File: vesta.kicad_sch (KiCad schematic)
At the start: 60 parts, among them J1 Solar Panel, J2 Solar Panel, J3 Conn_ARM_SWD_TagConnect_TC203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, U1 STM32WL55CCU6, U2 BQ24074RGTR, U3 TPS63900DSKR, U4 BME688_C3664478, U6 PE4259-63, X1 Q13FC1350000400, X2 X201632MMB4SI

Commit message: feat: updating the references and adding the logo
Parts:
- U2: footprint Package_DFN_QFN:MPS_QFN-16_3x3mm_P0.5mm -> JLCImport:BQ24074RGTR
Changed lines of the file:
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@@
 			)
 		)
-		(property "Footprint" "Package_DFN_QFN:MPS_QFN-16_3x3mm_P0.5mm"
+		(property "Footprint" "JLCImport:BQ24074RGTR"
 			(at 316.23 96.52 0)
 			(hide yes)

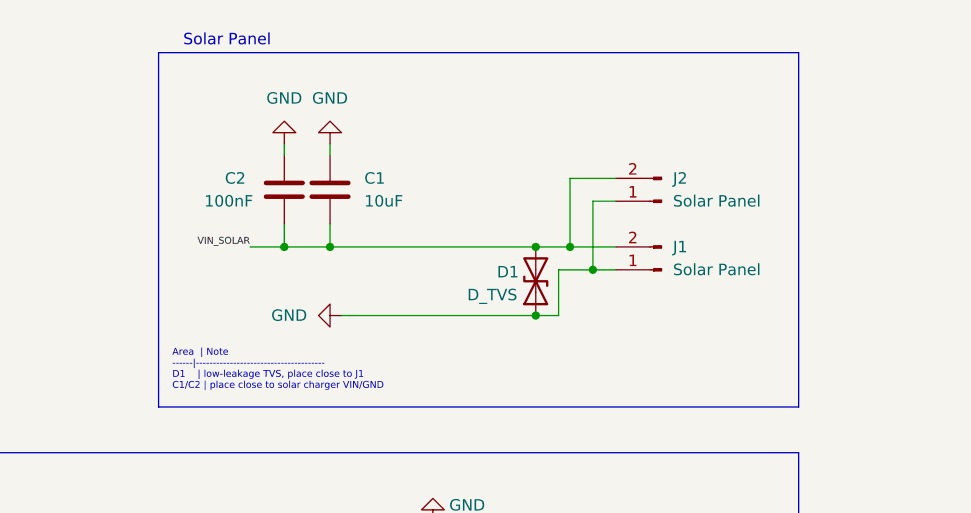
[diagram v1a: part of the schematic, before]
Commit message: feat: reverting the polarity on the batteries inputs
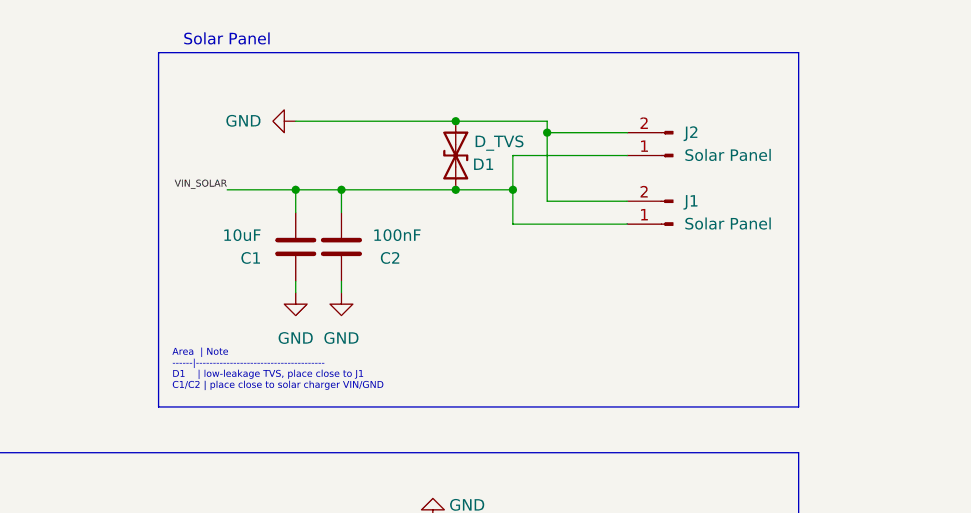
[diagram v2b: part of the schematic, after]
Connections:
- net GND: now also J1.2 (Pin_2), J2.2 (Pin_2); no longer J1.1 (Pin_1), J2.1 (Pin_1)
- net VIN_SOLAR: now also J1.1 (Pin_1), J2.1 (Pin_1); no longer J1.2 (Pin_2), J2.2 (Pin_2)
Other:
- moved on the sheet: C1, C2, D1, J1, J2

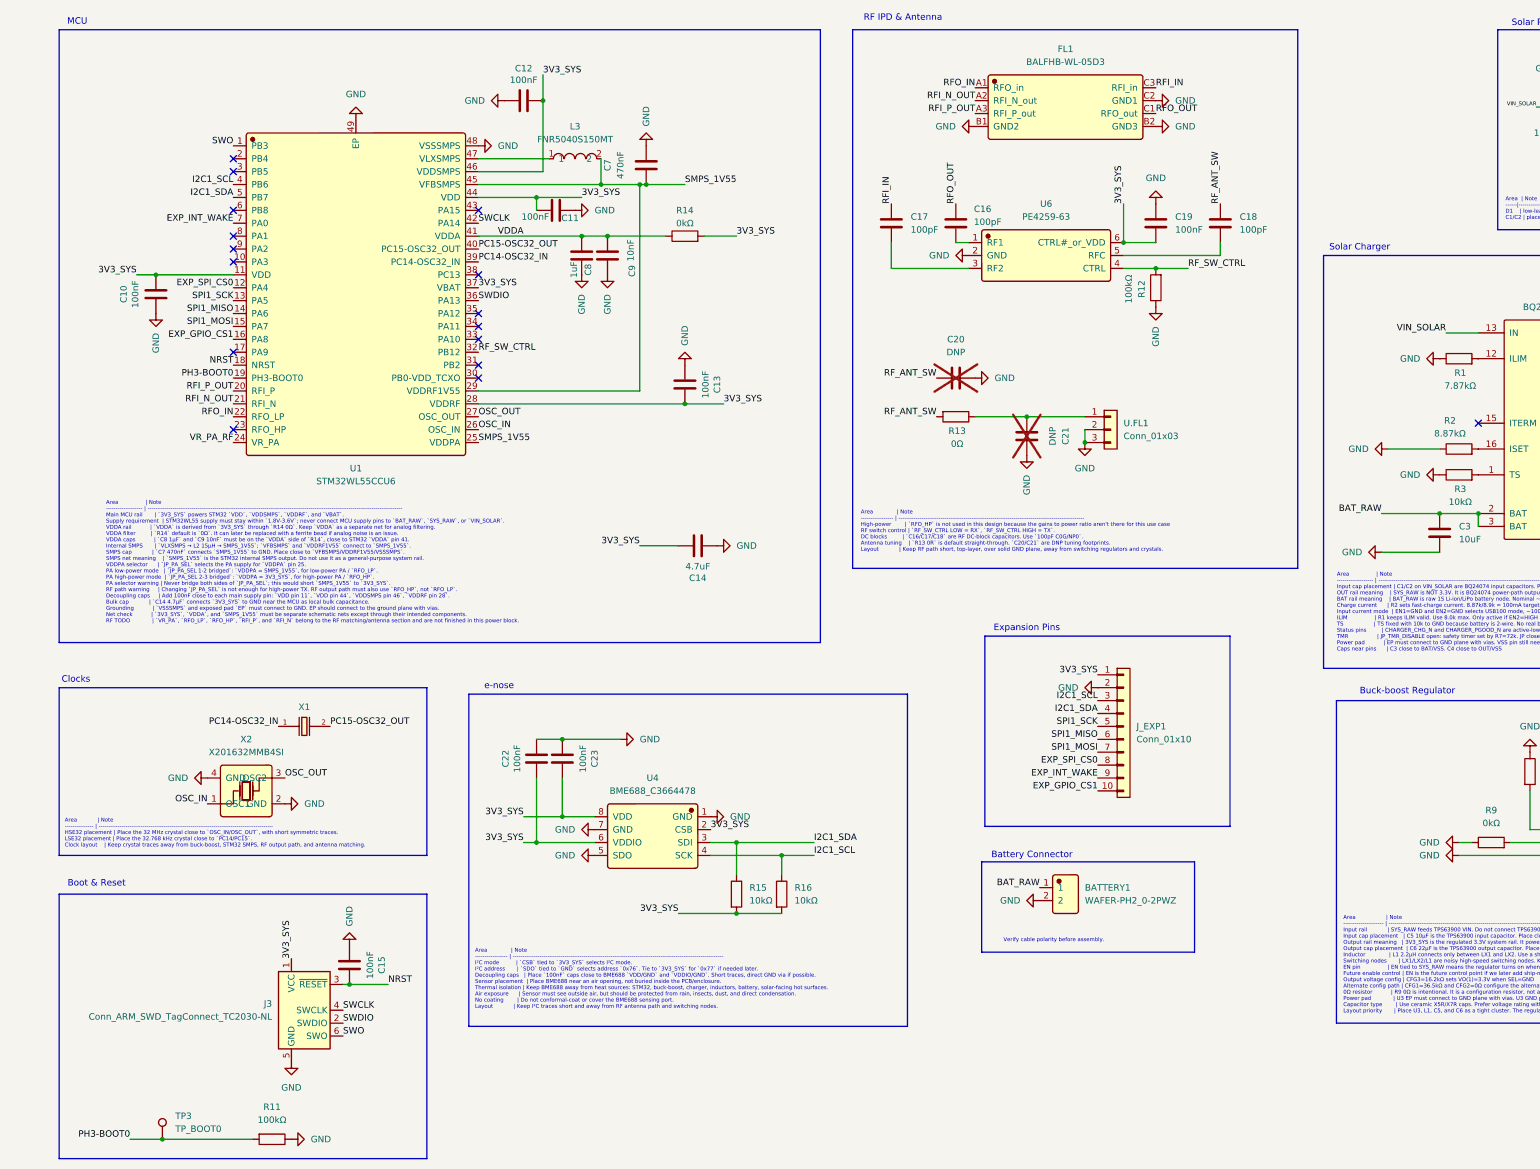
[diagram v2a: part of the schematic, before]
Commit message: feat: changing the MCU and antenna for a pre-certified module
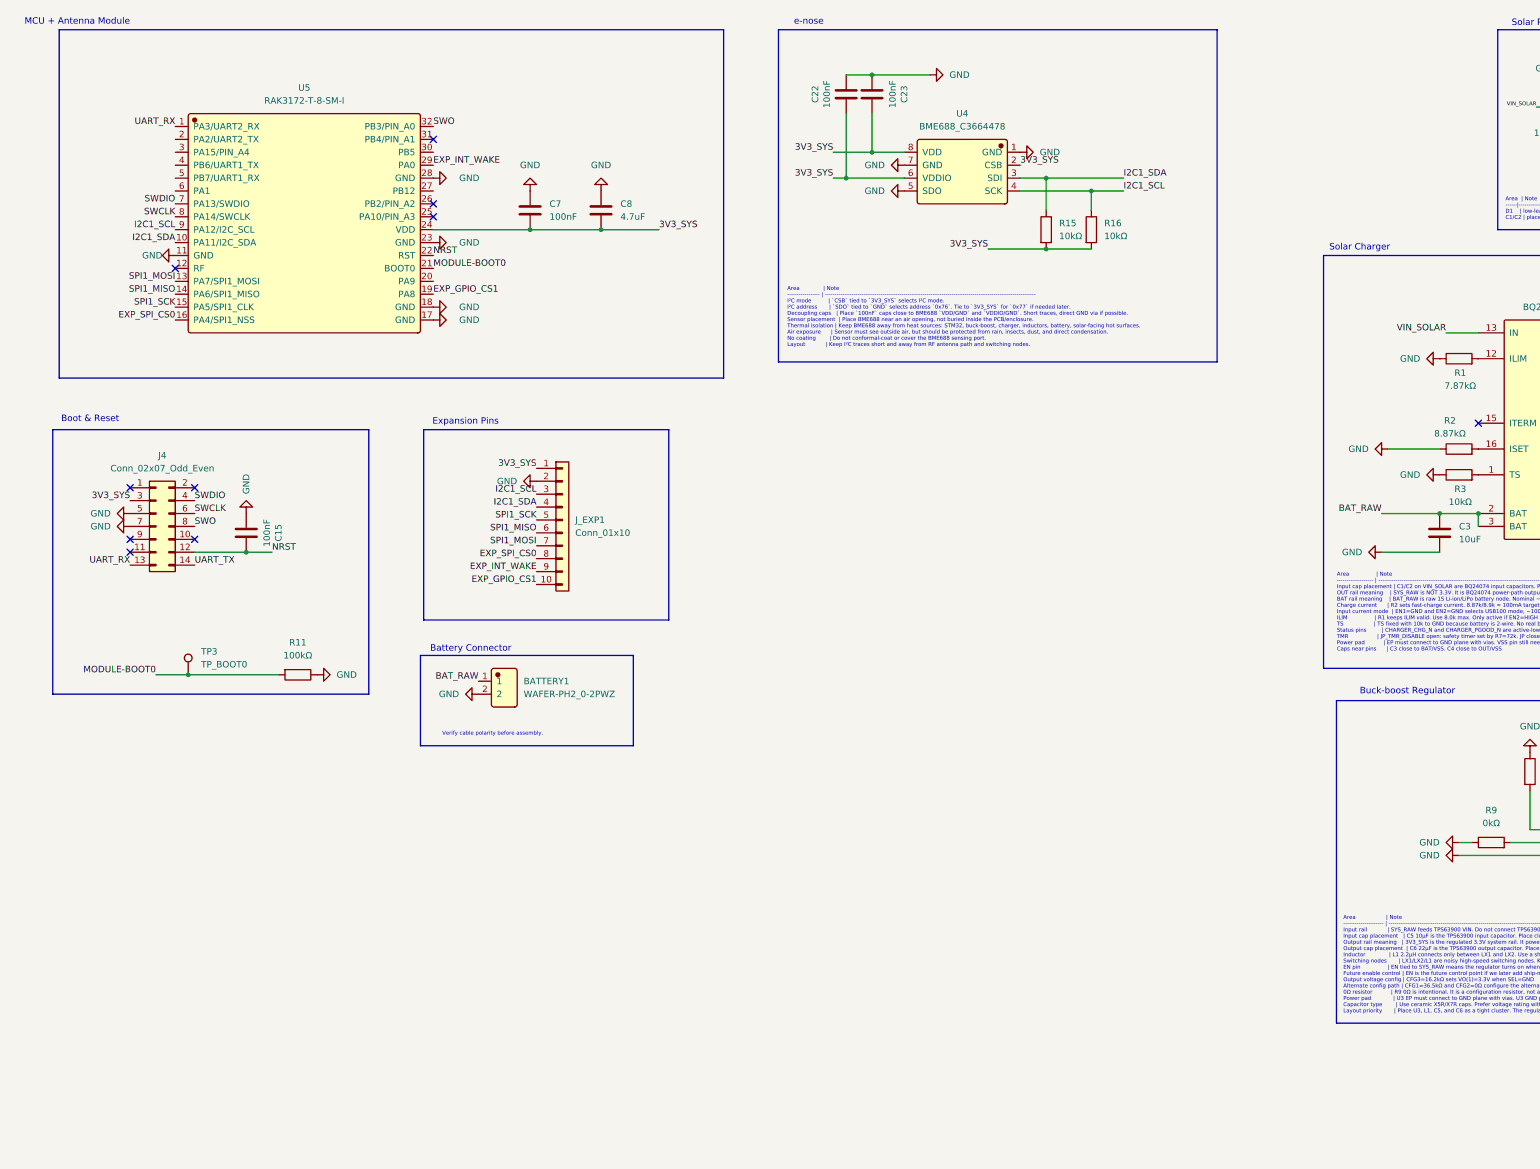
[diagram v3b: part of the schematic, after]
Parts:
- removed C10, C11, C12, C13, C19: 100nF, PCM_JLCPCB:C_0603, symbol Device:C
- removed C14: 4.7uF, PCM_JLCPCB:C_0805, symbol Device:C
- removed C16, C17, C18: 100pF, PCM_JLCPCB:C_0402, symbol Device:C
- removed C20, C21: DNP, Capacitor_SMD:C_0603_1608Metric, symbol Device:C
- removed C9: 10nF, PCM_JLCPCB:C_0603, symbol Device:C
- removed FL1: BALFHB-WL-05D3, JLCImport:BALFHB-WL-05D3, symbol JLCImport:BALFHB-WL-05D3
- removed J3: Conn_ARM_SWD_TagConnect_TC2030-NL, Connector:Tag-Connect_TC2030-IDC-NL_2x03_P1.27mm_Vertical, symbol Connector:Conn_ARM_SWD_TagConnect_TC2030-NL
- removed L3: FNR5040S150MT, JLCImport:FNR5040S150MT, symbol JLCImport:FNR5040S150MT
- removed R12: 100kΩ, PCM_JLCPCB:R_0603, symbol Device:R
- removed R13: 0Ω, PCM_JLCPCB:R_0402, symbol Device:R
- removed R14: 0kΩ, PCM_JLCPCB:R_0603, symbol Device:R
- removed U.FL1: Conn_01x03, PCM_JLCPCB:IPEX-SMD_BWIPX-1-001E, symbol Connector_Generic:Conn_01x03
- removed U1: STM32WL55CCU6, JLCImport:STM32WL55CCU6, symbol JLCImport:STM32WL55CCU6
- removed U6: PE4259-63, JLCImport:PE4259-63, symbol JLCImport:PE4259-63
- removed X1: Q13FC1350000400, PCM_JLCPCB:FC-135R_L3.2-W1.5, symbol PCM_JLCPCB-Crystals:Crystal, 32.768kHz, 13pF
- removed X2: X201632MMB4SI, JLCImport:X201632MMB4SI, symbol JLCImport:X201632MMB4SI
- added J4: Conn_02x07_Odd_Even, symbol Connector_Generic:Conn_02x07_Odd_Even
- added U5: RAK3172-T-8-SM-I, JLCImport:RAK3172-T-8-SM-I, symbol JLCImport:RAK3172-T-8-SM-I
- C7: value 470nF -> 100nF; footprint PCM_JLCPCB:C_0603 -> (none)
- C8: value 1uF -> 4.7uF; footprint PCM_JLCPCB:C_0603 -> (none)
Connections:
- net SMPS_1V55 is gone; now on net GND: C7.1
- net VDDA is gone; now on net GND: C8.1
- net 3V3_SYS: now also C7.2, C8.2, J4.3 (Pin_3), U5.24 (VDD)
- net EXP_GPIO_CS1: now also U5.19 (PA8)
- net EXP_INT_WAKE: now also U5.29 (PA0)
- net EXP_SPI_CS0: now also U5.16 (PA4/SPI1_NSS)
- net GND: now also J4.5 (Pin_5), J4.7 (Pin_7), U5.11 (GND), U5.17 (GND), U5.18 (GND), U5.23 (GND), U5.28 (GND); no longer C7.2, C8.2
- net I2C1_SCL: now also U5.9 (PA12/I2C_SCL)
- net I2C1_SDA: now also U5.10 (PA11/I2C_SDA)
- net NRST: now also J4.12 (Pin_12), U5.22 (RST)
- net SPI1_MISO: now also U5.14 (PA6/SPI1_MISO)
- net SPI1_MOSI: now also U5.13 (PA7/SPI1_MOSI)
- net SPI1_SCK: now also U5.15 (PA5/SPI1_CLK)
- net SWCLK: now also J4.6 (Pin_6), U5.8 (PA14/SWCLK)
- net SWDIO: now also J4.4 (Pin_4), U5.7 (PA13/SWDIO)
- net SWO: now also J4.8 (Pin_8), U5.32 (PB3/PIN_A0)
- net PH3-BOOT0 renamed MODULE-BOOT0
- net MODULE-BOOT0: now also U5.21 (BOOT0)
- new net UART_RX: J4.13 (Pin_13), U5.1 (PA3/UART2_RX)
- new net UART_TX: J4.14 (Pin_14)
- no-connect marks 16 -> 10
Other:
- note added: "MCU + Antenna Module"
- note removed: "Area | Note --------------- | ------------------------------------------------------------------------------------------- HSE32 placement | Place the 32 MHz crystal close to `OSC_IN/OSC_OUT`, with short symmetric traces. LSE32 placement | Place the 32.768 kHz crystal close to `PC14/PC15`. Clock layout | Keep crystal traces away from buck-boost, STM32 SMPS, RF output path, and antenna matching."
- note removed: "Area | Note ----------------- | ------------------------------------------------------------------------------------------------- High-power | `RFO_HP` is not used in this design because the gains to power ratio aren't there for this use case RF switch control | `RF_SW_CTRL LOW = RX`, `RF_SW_CTRL HIGH = TX`. DC blocks | `C16/C17/C18` are RF DC-block capacitors. Use `100pF C0G/NP0`. Antenna tuning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"
- note removed: "Area | Note ------------------- | ------------------------------------------------------------------------------------------------------------------------------------- Main MCU rail | `3V3_SYS` powers STM32 `VDD`, `VDDSMPS`, `VDDRF`, and `VBAT`. Supply requirement | STM32WL55 supply must stay within `1.8V-3.6V`; never connect MCU supply pins to `BAT_RAW`, `SYS_RAW`, or `VIN_SOLAR`. VDDA rail | `V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"
- note removed: "Clocks"
- note removed: "MCU"
- note removed: "RF IPD & Antenna"
- moved on the sheet: BATTERY1, C15, C22, C23, J_EXP1, R11, R15, R16, TP3, U4

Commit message: feat: adding the new components into the PCB
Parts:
- C7: footprint (none) -> Capacitor_SMD:C_01005_0402Metric
- C8: footprint (none) -> Capacitor_SMD:C_0805_2012Metric
- J4: footprint (none) -> Connector_PinHeader_1.27mm:PinHeader_2x07_P1.27mm_Vertical_SMD
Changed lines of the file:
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@@
 			)
 		)
-		(property "Footprint" ""
+		(property "Footprint" "Capacitor_SMD:C_01005_0402Metric"
 			(at 115.2652 57.15 0)
 			(hide yes)
@@
 			)
 		)
-		(property "Footprint" ""
+		(property "Footprint" "Connector_PinHeader_1.27mm:PinHeader_2x07_P1.27mm_Vertical_SMD"
 			(at 40.64 115.57 0)
 			(hide yes)
@@
 			)
 		)
-		(property "Footprint" ""
+		(property "Footprint" "Capacitor_SMD:C_0805_2012Metric"
 			(at 129.2352 57.15 0)
 			(hide yes)

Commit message: feat: small footprint fixes before starting the routing
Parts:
- C22, C23: footprint PCM_JLCPCB:C_0603 -> Capacitor_SMD:C_0402_1005Metric
- C7: footprint Capacitor_SMD:C_01005_0402Metric -> Capacitor_SMD:C_0402_1005Metric
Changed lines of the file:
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@@
 			)
 		)
-		(property "Footprint" "Capacitor_SMD:C_01005_0402Metric"
+		(property "Footprint" "Capacitor_SMD:C_0402_1005Metric"
 			(at 115.2652 57.15 0)
 			(hide yes)
@@
 			)
 		)
-		(property "Footprint" "PCM_JLCPCB:C_0603"
+		(property "Footprint" "Capacitor_SMD:C_0402_1005Metric"
 			(at 175.5648 26.67 0)
 			(hide yes)
@@
 			)
 		)
-		(property "Footprint" "PCM_JLCPCB:C_0603"
+		(property "Footprint" "Capacitor_SMD:C_0402_1005Metric"
 			(at 180.6448 26.67 0)
 			(hide yes)

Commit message: feat: PCB design ready
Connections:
- net UART_TX: now also U5.2 (PA2/UART2_TX)
- no-connect marks 10 -> 17
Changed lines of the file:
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@@
+	)
+	(no_connect
+		(at 44.45 49.53)
 	)
 	(no_connect
@@
 	)
 	(no_connect
+		(at 44.45 41.91)
+	)
+	(no_connect
 		(at 95.25 39.37)
 	)
@@
 	)
 	(no_connect
+		(at 44.45 46.99)
+	)
+	(no_connect
 		(at 35.56 118.11)
 	)
@@
 	)
 	(no_connect
+		(at 95.25 41.91)
+	)
+	(no_connect
+		(at 95.25 67.31)
+	)
+	(no_connect
 		(at 95.25 54.61)
+	)
+	(no_connect
+		(at 44.45 44.45)
+	)
+	(no_connect
+		(at 95.25 49.53)
 	)
 	(wire
@@
 		)
 	)
+	(label "UART_TX"
+		(at 44.45 39.37 180)
+		(effects
+			(font
+				(size 1.27 1.27)
+			)
+			(justify right bottom)
+		)
+	)

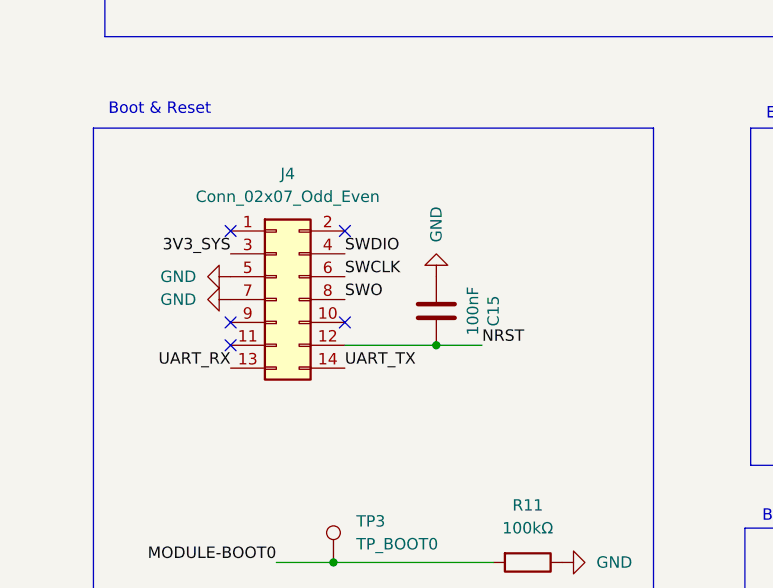
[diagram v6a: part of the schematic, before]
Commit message: feat: updaing the BOM and adding the STLINK connector
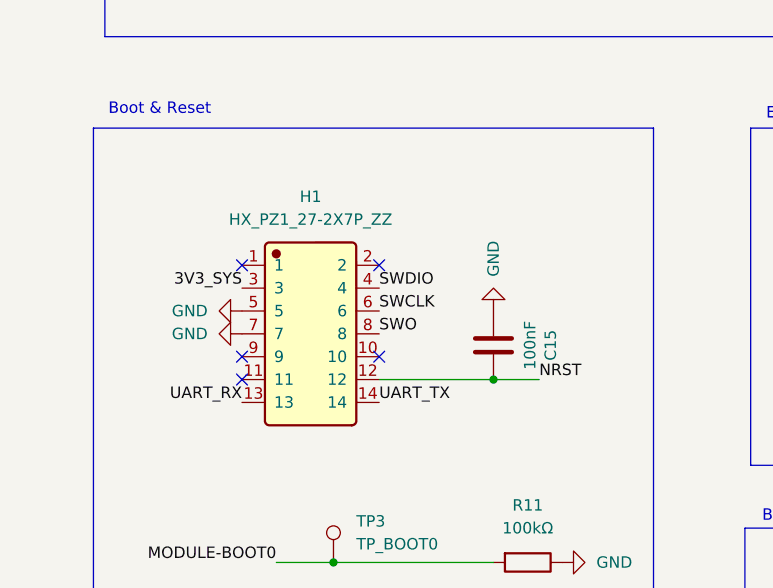
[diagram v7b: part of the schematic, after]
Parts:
- removed J4: Conn_02x07_Odd_Even, Connector_PinHeader_1.27mm:PinHeader_2x07_P1.27mm_Vertical_SMD, symbol Connector_Generic:Conn_02x07_Odd_Even
- added H1: HX_PZ1_27-2X7P_ZZ, JLCImport:HX_PZ1_27-2X7P_ZZ, symbol JLCImport:HX_PZ1_27-2X7P_ZZ
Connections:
- net 3V3_SYS: now also H1.3
- net GND: now also H1.5, H1.7
- net NRST: now also H1.12
- net SWCLK: now also H1.6
- net SWDIO: now also H1.4
- net SWO: now also H1.8
- net UART_RX: now also H1.13
- net UART_TX: now also H1.14
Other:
- moved on the sheet: C15

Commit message: chore: cleaning up the schematics
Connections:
- net 3V3_SYS: now also C22.2, C23.2, R15.1, R16.1, R5.2; no longer C22.1, C23.1, R15.2, R16.2, R5.1
- net CHARGER_CHG_N: now also R5.1; no longer R5.2
- net GND: now also C22.1, C23.1; no longer C22.2, C23.2
- net I2C1_SCL: now also R16.2; no longer R16.1
- net I2C1_SDA: now also R15.2; no longer R15.1
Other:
- moved on the sheet: C15, C22, C23, C4, C5, C6, C7, C8, JP_TMR_DISABLE1, L1, R10, R11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
